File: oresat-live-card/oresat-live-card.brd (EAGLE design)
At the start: 99.8 x 94.6 mm, 324 parts, among them J1 ORESAT-DEBUG-CONNECTOR-CARD, J100 DM3BT-DSF-PEJS, J102 FTSH-105-XX-X-DV-K, J2 SM06B-SRSS-TB(LF)(SN), J4 TFM-120-01-L-D-RA, Q1 MMBT2907, Q2 PMV45EN, Q3 DMP2240UDM, Q4 PMV45EN, Q5 MOSFET-PCH-SOT23-6, Q6 MOSFET-PCH-SOT23-6, U1 RCLAMP0504FB, U10 TLVH431, U11 TCAN330, U12 MIC842LYC5, U13 MIC842LYC5, U14 MAX4211FETE, U15 TPS62112, U16 MAX7310ATE, U17 25AAXX, U18 RCLAMP0504FB, U19 TQP9111, U2 TPS2051CDBVR, U3 THGBMJG7C2LBAU8, U4 SN74LVC1G07DCK, U5 TPS62112, U6 SN74LVC1G32QDBVRQ1, U7 OSD3358-512M-BSM, U8 MIC94090YC6-TR, Y1 24MHz, Y2 ABS07-32.768KHZ-T

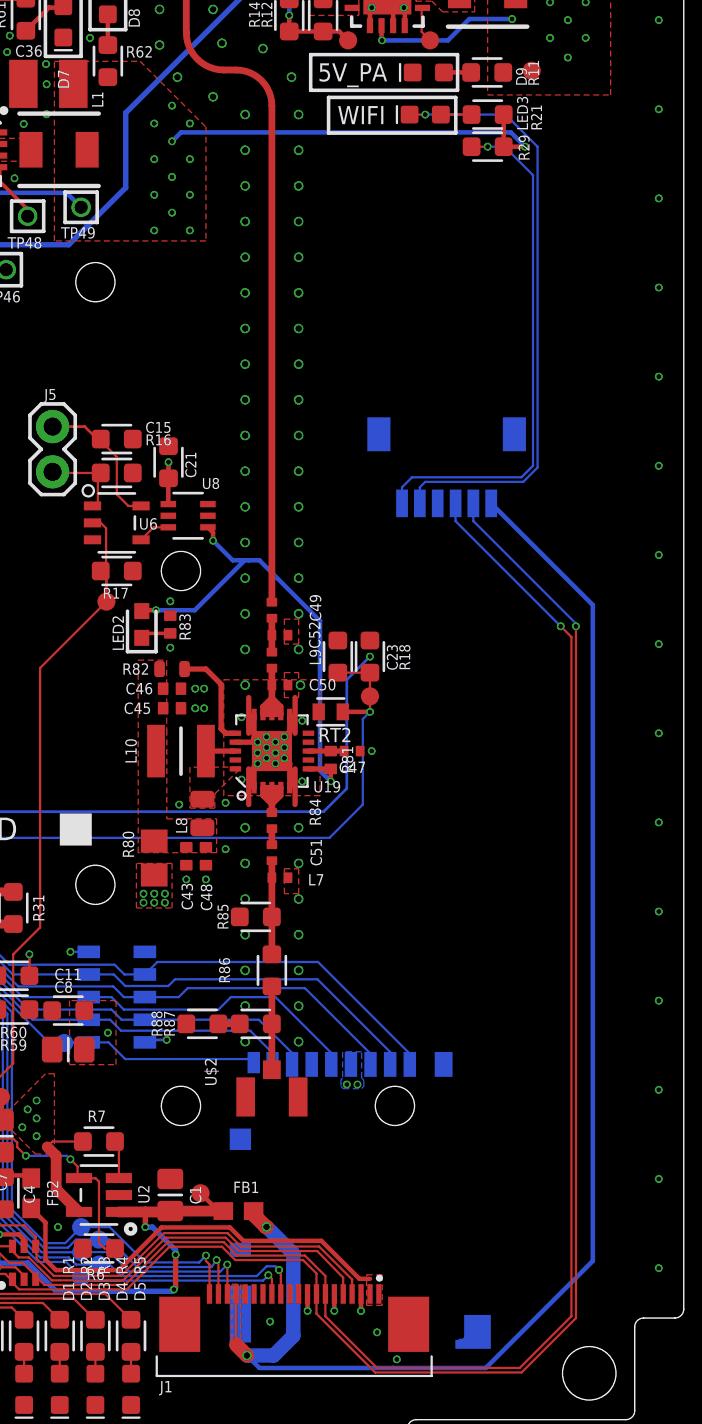
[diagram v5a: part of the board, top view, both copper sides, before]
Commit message: Added a silkscreen identifier for the PA enable LED
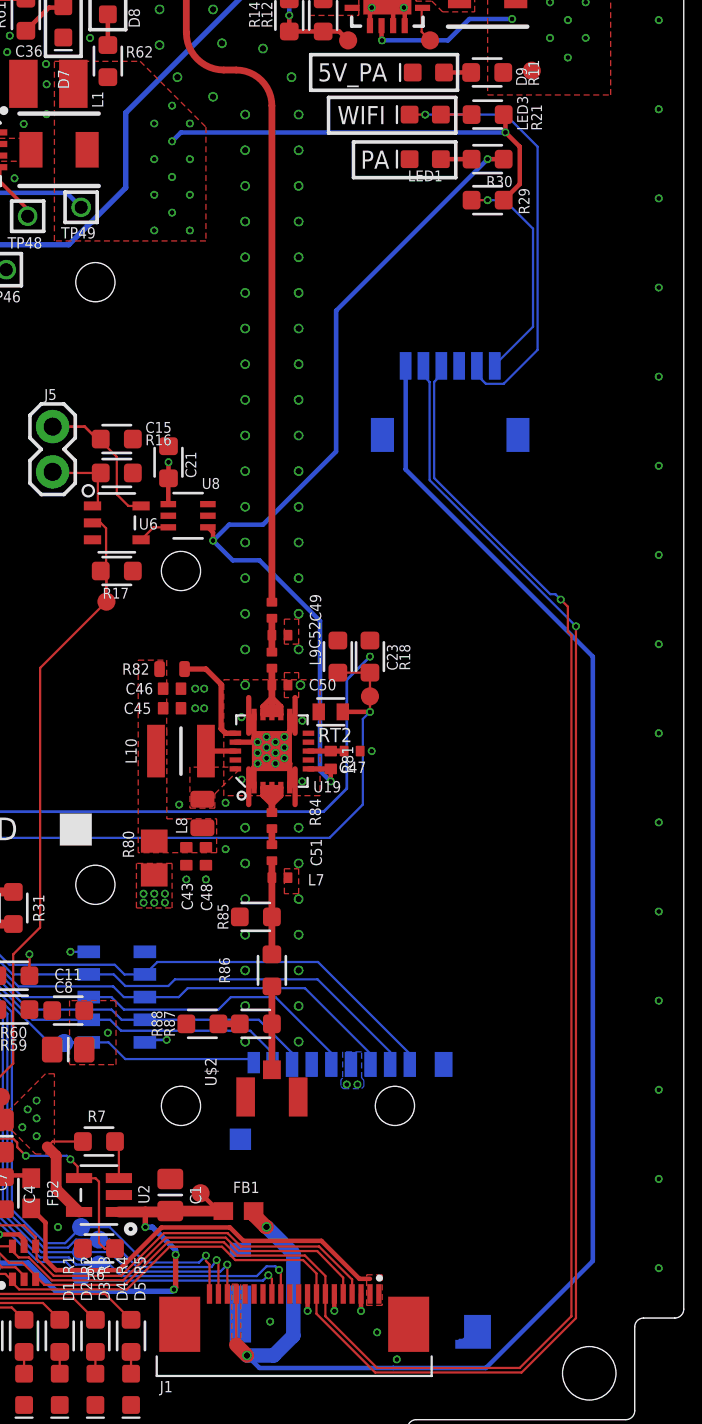
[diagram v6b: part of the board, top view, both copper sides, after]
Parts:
- removed LED2: LTST-C193KRKT-5A, oresat-samacsys_Parts:LEDC1607X80N
- removed R83: 1k, oresat-rcl:.0402-B-NOSILK
- added LED1: (no value), SparkFun-LED:LED-0603
- added R30: 1k, oresat-rcl:.0603-A
- moved R29 3.00 mm to (88.8, 71.3)
- moved J2 2.71 mm to (86.7, 59.5), turned to 0 degrees
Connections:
- removed net N$141: LED2.1, R83.2
- new net N$26: LED1.A, R30.2
- net GND: now also LED1.C; no longer R83.1
- net PA_TOGGLE: now also R30.1; no longer LED2.2
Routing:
- net PA_TOGGLE: track 26.9 -> 49.7 mm
- net WIFI_ENABLE: track 29.2 -> 12.7 mm
- net USB_HO_VBUS: track 81.7 -> 91.4 mm
- net WIFI_STATUS: track 33.9 -> 24.2 mm
- net USB_HO_N: track 104.4 -> 113.3 mm
- net USB_HO_P: track 105.0 -> 113.5 mm
- net N$26: track 0.00 -> 1.72 mm
- net N$141: track 1.70 -> 0.00 mm
- net 5V: track 113.7 -> 115.2 mm
- net GND: vias 261 -> 259
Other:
- board text added: "PA"

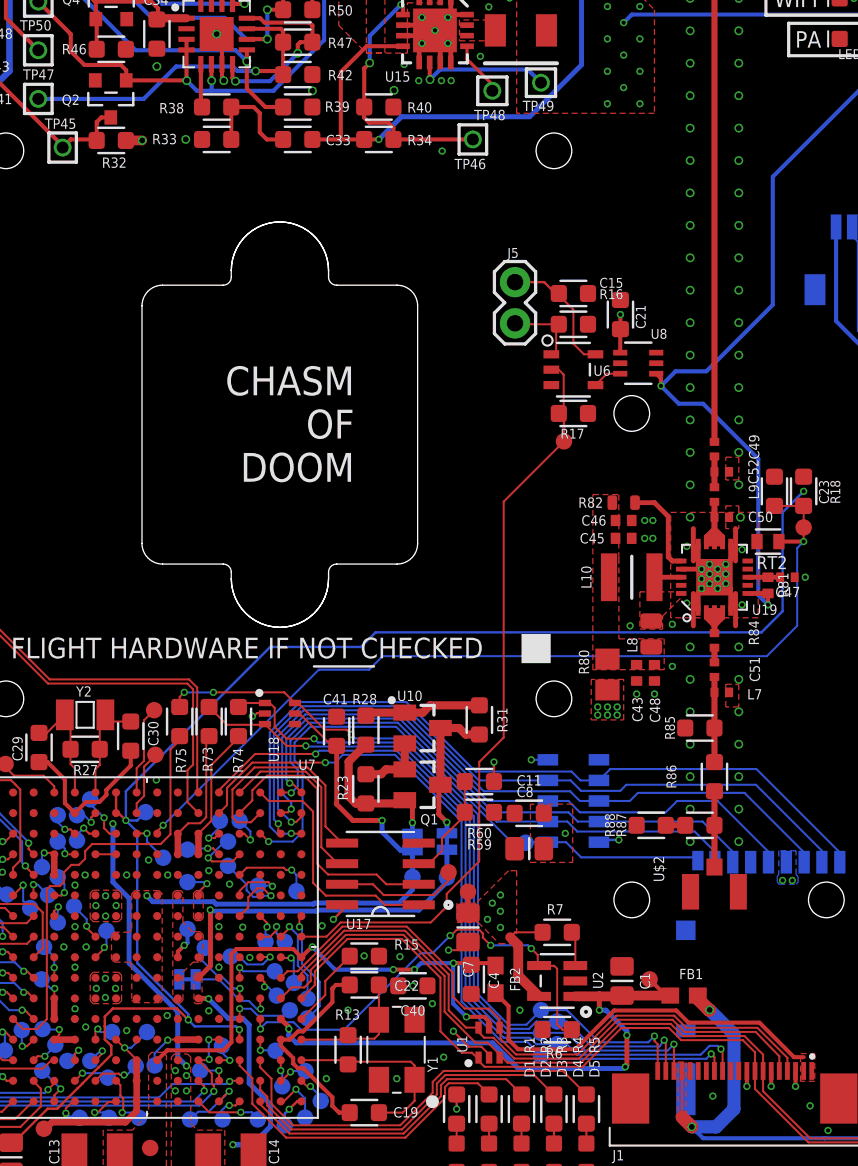
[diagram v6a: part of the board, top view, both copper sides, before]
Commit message: Added a 5V polygon. I'm not happy with it and will work on a better colution but it work for now
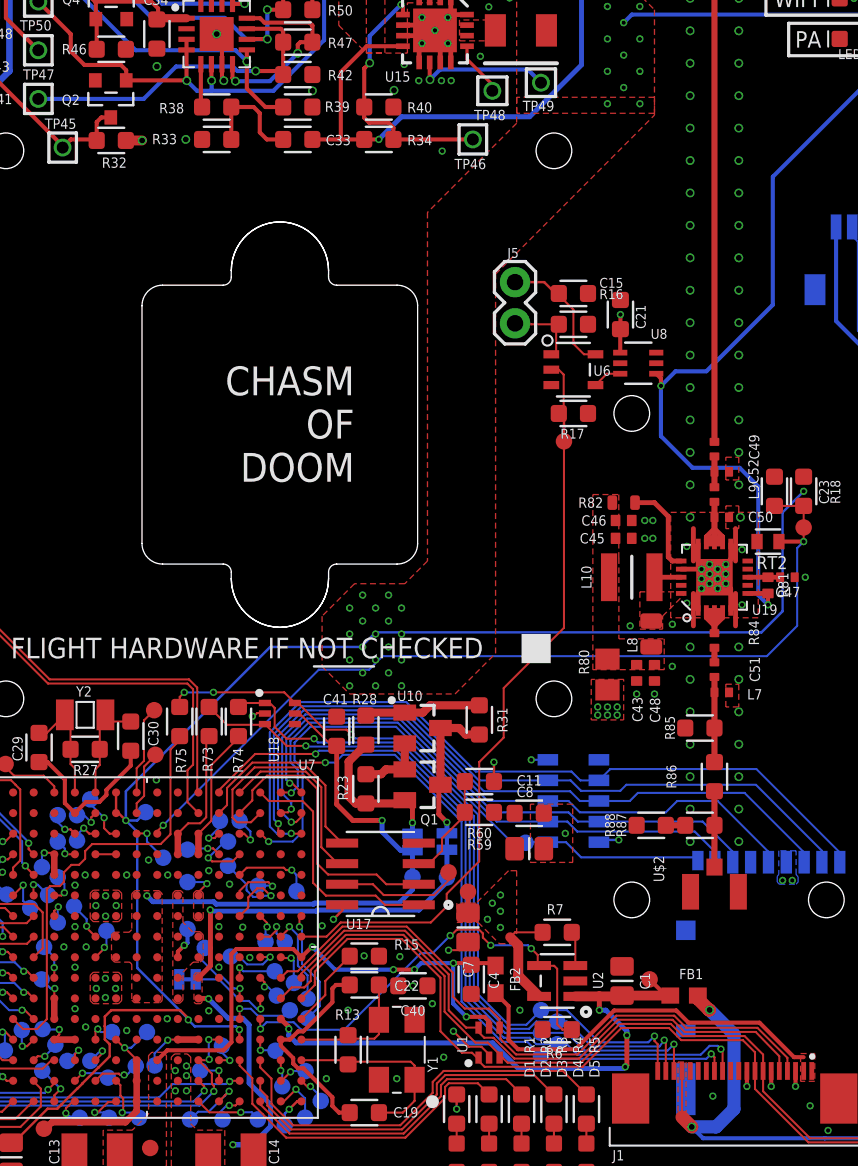
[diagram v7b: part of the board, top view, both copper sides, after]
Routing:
- net 5V: track 115.2 -> 33.4 mm, vias 20 -> 39
- net PA_TOGGLE: track 49.7 -> 50.5 mm
- net VDD: track 32.6 -> 33.1 mm
- added copper zone on layer 15, net 5V

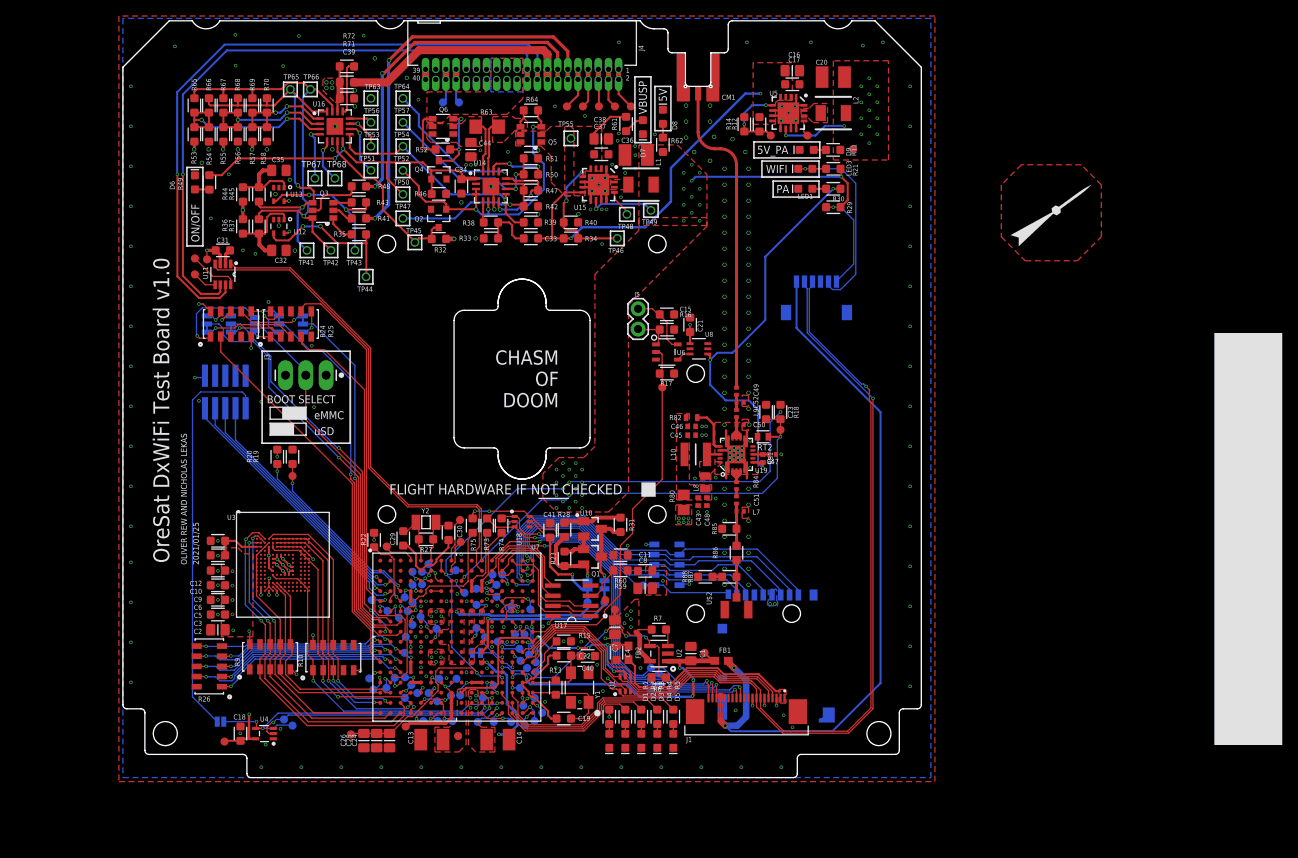
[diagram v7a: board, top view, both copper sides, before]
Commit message: reworked the 5V and 3.3V polygon routing
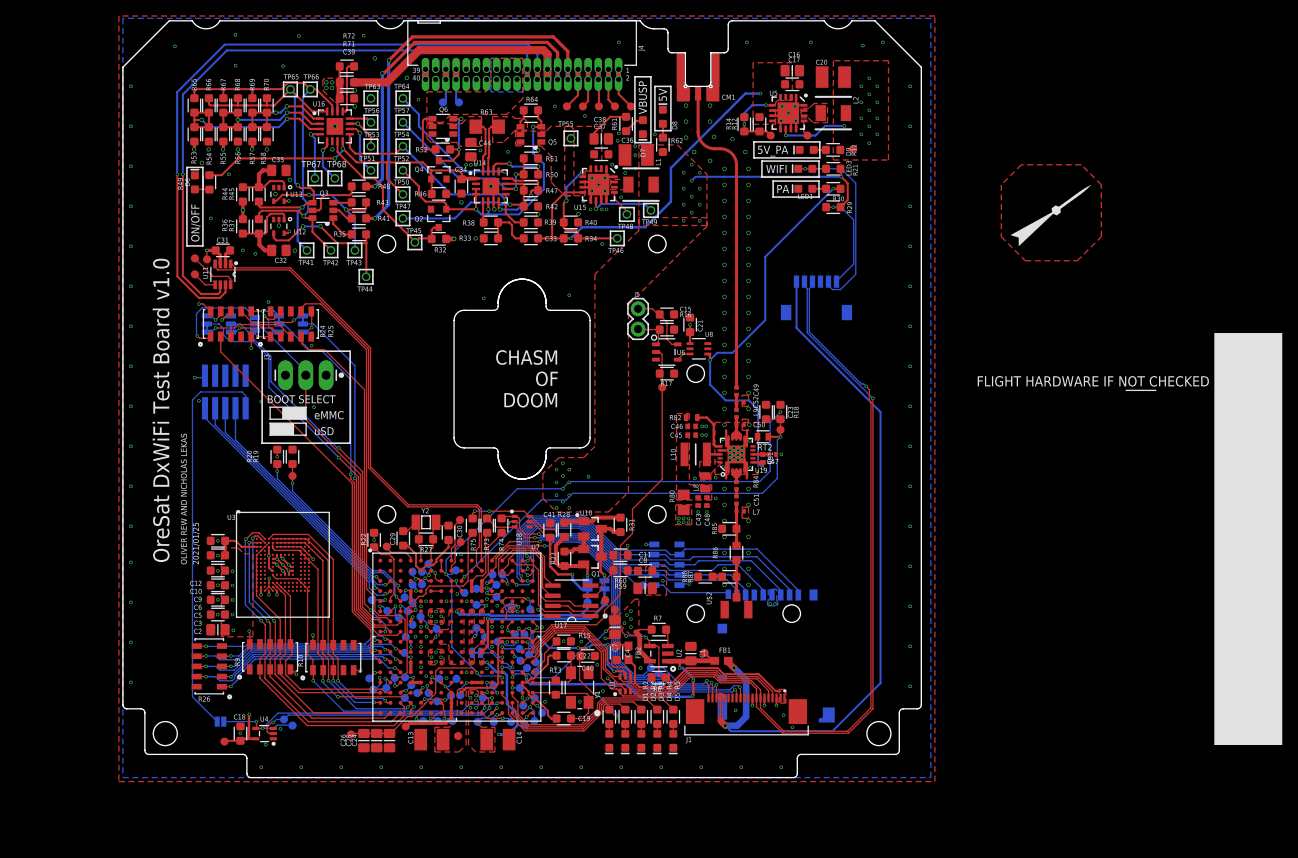
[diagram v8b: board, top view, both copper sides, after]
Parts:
- D6: value AMBER -> GREEN
- moved U$4 74.6 mm to (106.7, 48.9)
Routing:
- net VDD: track 33.1 -> 7.88 mm
- net 3.3V: track 41.8 -> 52.4 mm
- net N$97: track 1.81 -> 2.43 mm
- net GND: vias 259 -> 262
- net 5V: vias 39 -> 31
- added copper zone on layer 15, net VDD
